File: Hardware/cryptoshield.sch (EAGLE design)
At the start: 45 parts, among them J1 AVR_SPI_PRG_6PTH, Q1 BSS138, Q2 BSS138, Q3 BSS138, Q4 MOSFET-PCH, U1 33mhz

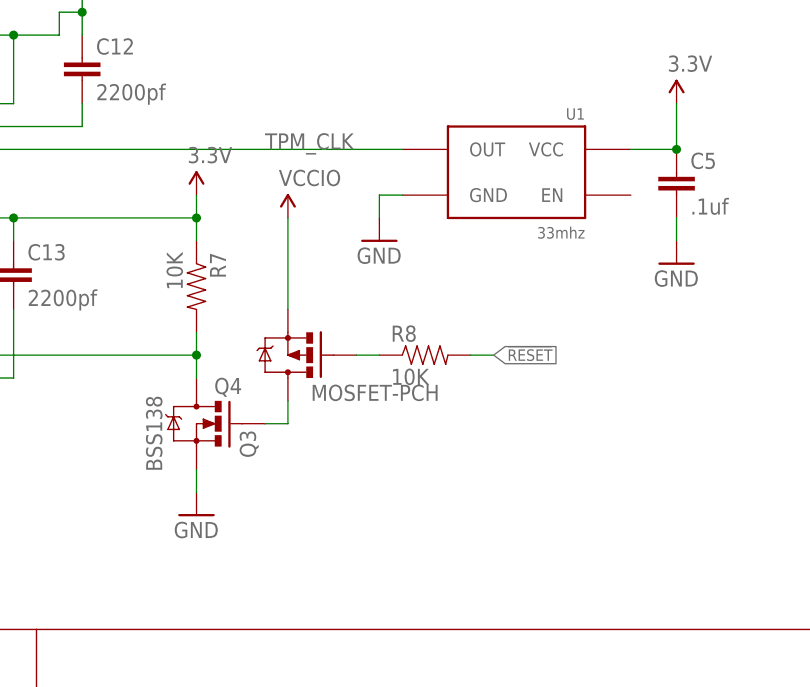
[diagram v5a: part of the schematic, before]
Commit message: made changed to isolate Reset from 5V
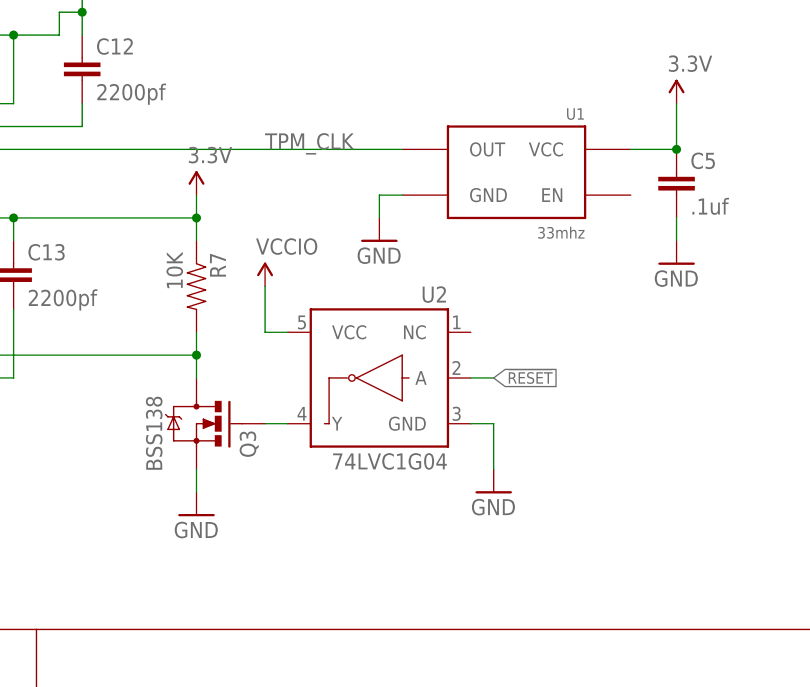
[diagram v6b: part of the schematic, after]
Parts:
- removed Q4: MOSFET-PCH, SparkFun-DiscreteSemi:MOSFET-PCHANNEL
- removed R8: 10K, SparkFun:RESISTOR0603-RES
- added U2: 74LVC1G04, SparkFun-DigitalIC:INVERTER_SOT353-5
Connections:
- removed net N$21: Q4.G, R8.1
- net !RESET: now also U2.A; no longer R8.2
- net GND: now also U2.GND
- net N$20: now also U2.Y; no longer Q4.D
- net VCCIO: now also U2.VCC; no longer Q4.S
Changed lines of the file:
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@@
 <layer number="56" name="wert" color="7" fill="1" visible="no" active="no"/>
 <layer number="57" name="tCAD" color="7" fill="1" visible="no" active="no"/>
+<layer number="90" name="Modules" color="5" fill="1" visible="yes" active="yes"/>
 <layer number="91" name="Nets" color="2" fill="1" visible="yes" active="yes"/>
 <layer number="92" name="Busses" color="1" fill="1" visible="yes" active="yes"/>
@@
 <layer number="251" name="SMDround" color="12" fill="11" visible="no" active="no"/>
 <layer number="254" name="cooling" color="7" fill="1" visible="no" active="yes"/>
+<layer number="255" name="routoute" color="7" fill="1" visible="yes" active="yes"/>
 </layers>
 <schematic xreflabel="%F%N/%S.%C%R" xrefpart="/%S.%C%R">
@@
 <part name="R7" library="SparkFun" deviceset="RESISTOR" device="0603-RES" value="10K"/>
 <part name="GND10" library="supply1" deviceset="GND" device=""/>
-<part name="Q4" library="SparkFun-DiscreteSemi" deviceset="MOSFET-PCHANNEL" device="" value="MOSFET-PCH"/>
 <part name="SUPPLY20" library="SparkFun-Aesthetics" deviceset="VCCIO" device=""/>
-<part name="R8" library="SparkFun" deviceset="RESISTOR" device="0603-RES" value="10K"/>
+<part name="U2" library="SparkFun-DigitalIC" deviceset="INVERTER" device="_SOT353-5" value="74LVC1G04"/>
+<part name="GND12" library="supply1" deviceset="GND" device=""/>
 </parts>
 <sheets>
@@
 <instance part="R7" gate="G$1" x="304.8" y="226.06" rot="R270"/>
 <instance part="GND10" gate="1" x="304.8" y="200.66"/>
-<instance part="Q4" gate="G$1" x="314.96" y="218.44" smashed="yes" rot="R180">
-<attribute name="NAME" x="309.88" y="215.9" size="1.778" layer="95" rot="R180"/>
-<attribute name="VALUE" x="317.5" y="213.36" size="1.778" layer="96"/>
-</instance>
-<instance part="SUPPLY20" gate="G$1" x="314.96" y="233.68"/>
-<instance part="R8" gate="G$1" x="330.2" y="218.44"/>
+<instance part="SUPPLY20" gate="G$1" x="312.42" y="226.06"/>
+<instance part="U2" gate="G$1" x="325.12" y="215.9" rot="MR0"/>
+<instance part="GND12" gate="1" x="337.82" y="203.2"/>
 </instances>
 <busses>
@@
 <wire x1="304.8" y1="203.2" x2="304.8" y2="205.74" width="0.1524" layer="91"/>
 </segment>
+<segment>
+<pinref part="U2" gate="G$1" pin="GND"/>
+<pinref part="GND12" gate="1" pin="GND"/>
+<wire x1="335.28" y1="210.82" x2="337.82" y2="210.82" width="0.1524" layer="91"/>
+<wire x1="337.82" y1="210.82" x2="337.82" y2="205.74" width="0.1524" layer="91"/>
+</segment>
 </net>
 <net name="VBAT" class="0">
@@
 </segment>
 <segment>
-<pinref part="Q4" gate="G$1" pin="S"/>
 <pinref part="SUPPLY20" gate="G$1" pin="VCCIO"/>
-<wire x1="314.96" y1="233.68" x2="314.96" y2="223.52" width="0.1524" layer="91"/>
+<wire x1="312.42" y1="226.06" x2="312.42" y2="220.98" width="0.1524" layer="91"/>
+<pinref part="U2" gate="G$1" pin="VCC"/>
+<wire x1="312.42" y1="220.98" x2="314.96" y2="220.98" width="0.1524" layer="91"/>
 </segment>
 </net>
@@
 </segment>
 </net>
-<net name="N$20" class="0">
-<segment>
-<pinref part="Q3" gate="G$1" pin="G"/>
-<pinref part="Q4" gate="G$1" pin="D"/>
-<wire x1="312.42" y1="210.82" x2="314.96" y2="210.82" width="0.1524" layer="91"/>
-<wire x1="314.96" y1="210.82" x2="314.96" y2="213.36" width="0.1524" layer="91"/>
-</segment>
-</net>
-<net name="N$21" class="0">
-<segment>
-<pinref part="Q4" gate="G$1" pin="G"/>
-<pinref part="R8" gate="G$1" pin="1"/>
-<wire x1="325.12" y1="218.44" x2="322.58" y2="218.44" width="0.1524" layer="91"/>
-</segment>
-</net>
 <net name="!RESET" class="0">
 <segment>
-<pinref part="R8" gate="G$1" pin="2"/>
-<wire x1="335.28" y1="218.44" x2="337.82" y2="218.44" width="0.1524" layer="91"/>
-<label x="337.82" y="218.44" size="1.27" layer="95" xref="yes"/>
+<wire x1="335.28" y1="215.9" x2="337.82" y2="215.9" width="0.1524" layer="91"/>
+<label x="337.82" y="215.9" size="1.27" layer="95" xref="yes"/>
+<pinref part="U2" gate="G$1" pin="A"/>
 </segment>
 <segment>
@@
 </segment>
 </net>
+<net name="N$20" class="0">
+<segment>
+<pinref part="Q3" gate="G$1" pin="G"/>
+<pinref part="U2" gate="G$1" pin="Y"/>
+<wire x1="314.96" y1="210.82" x2="312.42" y2="210.82" width="0.1524" layer="91"/>
+</segment>
+</net>

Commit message: modified layout to meet checklist compliance
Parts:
- removed FRAME1: FRAME-LEDGER, SparkFun-Aesthetics:FRAME-LEDGER
- removed JP4: (no value), SparkFun-Connectors:M06NO_SILK
- removed S1: (no value), SparkFun-Electromechanical:TAC_SWITCHSMD
- removed SJ1, SJ2: JUMPER-PAD-2-NOYES_SILK, SparkFun-Passives:JUMPER-PAD-2-NOYES_SILK
- removed U$1: ARDUINO_R3_SHIELD, SparkFun-Boards:ARDUINO_R3_SHIELD
- removed U$8: ID-12/20SMD, SparkFun-RF:ID-12/20SMD
- added FRAME2: (no value), SparkFun-Aesthetics:FRAME-LETTER
- added JP3: (no value), SparkFun-Connectors:M06NO_SILK
- added S2: Reset, SparkFun-Electromechanical:SWITCH-MOMENTARY-2SMD
- added SJ100, SJ101: JUMPER-PAD-2-NOYES_SILK, SparkFun-Passives:JUMPER-PAD-2-NOYES_SILK
- added U3: ID-12/20SMD, SparkFun-RF:ID-12/20SMD
- added U4: ARDUINO_R3_SHIELD, SparkFun-Boards:ARDUINO_R3_SHIELD
- AES1: device cryptotronix:ATAES132 -> SparkFun-DigitalIC:ATAES132
- C1: value 10uF -> 0.1uF; device SparkFun-Capacitors:10UF50V20%(1210) -> SparkFun-Capacitors:0.1UF-25V(+80/-20%)(0603)
- C10, C4: value 0.1uF -> .1uf
- C12, C7: value 2200pf -> 0.1uF; device SparkFun-Capacitors:2.2NF/2200PF-50V-10%(0603) -> SparkFun-Capacitors:0.1UF-25V(+80/-20%)(0603)
- C13: value 2200pf -> 10uF; device SparkFun-Capacitors:2.2NF/2200PF-50V-10%(0603) -> SparkFun-Capacitors:10UF50V20%(1210)
- C2: value .1uf -> 0.1uF
- C5: value .1uf -> 2200pf; device SparkFun-Capacitors:0.1UF-25V(+80/-20%)(0603) -> SparkFun-Capacitors:2.2NF/2200PF-50V-10%(0603)
- C6, C9: value 0.1uF -> 2200pf; device SparkFun-Capacitors:0.1UF-25V(+80/-20%)(0603) -> SparkFun-Capacitors:2.2NF/2200PF-50V-10%(0603)
- ECC1: device cryptotronix:ATECC108 -> SparkFun-DigitalIC:ATECC108
- R1: value 10K -> 1k; device SparkFun:RESISTOR0603-RES -> SparkFun-Resistors:1K-1%
- R2: value 1k -> 10K; device SparkFun-Resistors:1K-1% -> SparkFun-Resistors:10KOHM-1/10W-1%(0603)0603
- R3: value 10K -> 4.7K; device SparkFun:RESISTOR0603-RES -> SparkFun-Resistors:4.7KOHM1/10W1%(0603)
- R4, R5, R7: device SparkFun:RESISTOR0603-RES -> SparkFun-Resistors:10KOHM-1/10W-1%(0603)0603
- R6: value 4.7K -> 10K; device SparkFun-Resistors:4.7KOHM1/10W1%(0603) -> SparkFun-Resistors:10KOHM-1/10W-1%(0603)0603
- RTC1: device cryptotronix:DS3231M -> SparkFun-DigitalIC:DS3231M
- SHA1: value ATSHA204 -> ATSHA204_SOIC8; device cryptotronix:ATSHA204 -> SparkFun-DigitalIC:ATSHA204_SOIC8
- TPM1: device cryptotronix:AT97SC3204T -> SparkFun-DigitalIC:AT97SC3204T
- U1: value 33mhz -> 74LVC1G04; device cryptotronix:OSCILLATOR -> SparkFun-DigitalIC:INVERTER_SOT353-5
- U2: value 74LVC1G04 -> 33mhz; device SparkFun-DigitalIC:INVERTER_SOT353-5 -> SparkFun-FreqCtrl:33MHZ-OSCILLATOR
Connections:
- removed net AUTH0: AES1.AUTHO
- net !RESET: now also U1.A, U4.RES; no longer U$1.RES, U2.A
- net 3.3V: now also C1.1, C10.1, JP3.6, Q3.G, R2.1, R3.2, R4.1, R5.1, U2.VCC, U4.3.3V; no longer C12.1, C13.1, JP4.6, Q1.G, R1.1, R3.1, R6.2, R7.1, U$1.3.3V, U1.VCC
- net ANT1: now also JP3.3, U3.ANT1; no longer JP4.3, U$8.ANT1
- net ANT2: now also JP3.4, U3.ANT2; no longer JP4.4, U$8.ANT2
- net GND: now also JP3.5, Q1.S, S2.1, U3.+/-, U3.GNDT, U4.GND@0, U4.GND@1, U4.GND@2; no longer JP4.5, Q3.S, S1.1, S1.2, U$1.GND@0, U$1.GND@1, U$1.GND@2, U$8.+/-, U$8.GNDT
- net N$1: now also R1.2, U3.LED; no longer R2.2, U$8.LED
- net N$12: now also R1.1; no longer R2.1
- net N$18: now also Q1.D, R2.2; no longer Q3.D, R7.2
- net N$19: now also R3.1; no longer R6.1
- net N$20: now also Q1.G, U1.Y; no longer Q3.G, U2.Y
- net N$4: now also SJ101.2, U4.A4; no longer SJ1.2, U$1.A4
- net N$6: now also SJ100.2, U4.A5; no longer SJ2.2, U$1.A5
- net PP: now also S2.2; no longer S1.3, S1.4
- net RX: now also U3.D0, U4.RX; no longer U$1.RX, U$8.D0
- net SCL: now also JP3.2, Q3.S, R5.2; no longer JP4.2, Q2.S, R1.2
- net SCL_IN: now also Q3.D, R7.2, SJ100.1, U4.SCL; no longer Q2.D, R5.2, SJ2.1, U$1.SCL
- net SDA: now also JP3.1, Q2.S, R4.2; no longer JP4.1, Q1.S, R3.2
- net SDA_IN: now also Q2.D, R6.2, SJ101.1, U4.SDA; no longer Q1.D, R4.2, SJ1.1, U$1.SDA
- net TPM_CLK: now also U2.OUT; no longer U1.OUT
- net VCCIO: now also C12.1, C13.1, R6.1, R7.1, U1.VCC, U3.5V, U3.RES, U4.IOREF; no longer C1.1, C10.1, R4.1, R5.1, U$1.IOREF, U$8.5V, U$8.RES, U2.VCC
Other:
- note added: "Real Time Clock"
- note removed: "AVR ISCP"
- note removed: "Josh Datko / Casey Kuhns"
- note removed: "Real Time Clock (w/ Battery)"
- note removed: "Revision History: v01: Initial v02: Changed 5V to IOREF"
- note removed: "v02"
- moved on the sheet: AES1, BAT1, C1, C10, C11, C12, C13, C2, C3, C4, C5, C6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

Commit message: fixed all github issues
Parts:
- removed AES1: ATAES132, SparkFun-DigitalIC:ATAES132
- removed D1: GREEN, SparkFun-LED:LED-GREEN0603
- removed ECC1: ATECC108, SparkFun-DigitalIC:ATECC108
- removed RTC1: DS3231M, SparkFun-DigitalIC:DS3231M
- removed SHA1: ATSHA204_SOIC8, SparkFun-DigitalIC:ATSHA204_SOIC8
- removed SJ100, SJ101: JUMPER-PAD-2-NOYES_SILK, SparkFun-Passives:JUMPER-PAD-2-NOYES_SILK
- removed TPM1: AT97SC3204T, SparkFun-DigitalIC:AT97SC3204T
- added A4, A5: JUMPER-PAD-2-NOYES_SILK, SparkFun-Passives:JUMPER-PAD-2-NOYES_SILK
- added LOGO2: OSHW-LOGOS, SparkFun-Aesthetics:OSHW-LOGOS
- added LOGO3: SFE_LOGO_NAME_FLAME.1_INCH, SparkFun-Aesthetics:SFE_LOGO_NAME_FLAME.1_INCH
- added STAT: GREEN, SparkFun-LED:LED-GREEN0603
- added U5: ATAES132, SparkFun-DigitalIC:ATAES132
- added U6: AT97SC3204T, SparkFun-DigitalIC:AT97SC3204T
- added U7: DS3231M, SparkFun-DigitalIC:DS3231M
- added U8: ATSHA204_SOIC8, SparkFun-DigitalIC:ATSHA204_SOIC8
- added U9: ATECC108, SparkFun-DigitalIC:ATECC108
- FRAME2: VERSION v10 -> v02
- JP3: device SparkFun-Connectors:M06NO_SILK -> SparkFun-Connectors:M06NO_SILK_FEMALE_PTH
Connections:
- net 3.3V: now also U5.VCC, U6.ATEST4, U6.ATEST8, U6.SB3V, U6.VCC1, U6.VCC2, U6.VCC3, U7.VCC, U8.VCC, U9.VCC; no longer AES1.VCC, ECC1.VCC, RTC1.VCC, SHA1.VCC, TPM1.ATEST4, TPM1.ATEST8, TPM1.SB3V, TPM1.VCC1, TPM1.VCC2, TPM1.VCC3
- net 32KHZ: now also U7.32KHZ; no longer RTC1.32KHZ
- net GND: now also STAT.C, U5.GND, U6.ATEST0, U6.ATEST1, U6.ATEST2, U6.ATEST3, U6.ATEST5, U6.ATEST6, U6.GND, U6.GND0, U6.GND1, U6.GND3, U6.TESTBI, U6.TESTTI, U7.GND, U8.GND, U9.GND; no longer AES1.GND, D1.C, ECC1.GND, RTC1.GND, SHA1.GND, TPM1.ATEST0, TPM1.ATEST1, TPM1.ATEST2, TPM1.ATEST3, TPM1.ATEST5, TPM1.ATEST6, TPM1.GND, TPM1.GND0, TPM1.GND1, TPM1.GND3, TPM1.TESTBI, TPM1.TESTTI
- net N$12: now also STAT.A; no longer D1.A
- net N$18: now also U6.RST; no longer TPM1.RST
- net N$19: now also U6.ATEST7; no longer TPM1.ATEST7
- net N$4: now also A4.2; no longer SJ101.2
- net N$6: now also A5.2; no longer SJ100.2
- net PP: now also U7.RST; no longer RTC1.RST
- net SCL: now also U5.SCL, U6.SCL, U7.SCL, U8.SCL, U9.SCL; no longer AES1.SCL, ECC1.SCL, RTC1.SCL, SHA1.SCL, TPM1.SCL
- net SCL_IN: now also A5.1; no longer SJ100.1
- net SDA: now also U5.SDA, U6.SDA, U7.SDA, U8.SDA, U9.SDA; no longer AES1.SDA, ECC1.SDA, RTC1.SDA, SHA1.SDA, TPM1.SDA
- net SDA_IN: now also A4.1; no longer SJ101.1
- net SQW: now also U7.SQW; no longer RTC1.SQW
- net TPM_CLK: now also U6.CLK; no longer TPM1.CLK
- net VBAT: now also U7.VBAT; no longer RTC1.VBAT
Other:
- note added: "Close Jumpers for older than R3 Arduinos"
- moved on the sheet: BAT1, C1, C10, C11, C12, C13, C2, C3, C4, C5, C6, C7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
